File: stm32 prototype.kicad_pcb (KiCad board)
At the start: 2 copper layers, 109 parts, among them J1 USB_B_Mini, J2 Conn_01x06_Male, J3 Conn_01x02, Q1 Q_NMOS_GSD, Q2 Q_NMOS_GSD, Q3 Q_NMOS_GSD, Q4 Q_NMOS_GSD, Q5 Q_NMOS_GSD, Q6 Q_NMOS_GSD, Q7 Q_NMOS_GSD, Q8 Q_NMOS_GSD, Q9 Q_NMOS_GSD, U1 FT232RL, U2 W25Q128JV-DTR, U3 STM32F407VGTx, U4 LD1117S33TR, U5 ESP32, U6 IS25LP016D-JNLE-TR, Y1 Crystal_GND24, Y2 Crystal_GND23, Y3 Crystal_GND23

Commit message: worked on some layout
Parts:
- added C16: 2.2uF, Capacitors_SMD:C_0603, F.Cu at (175.5, 142.2)
- added C38: 2.2uF, Capacitors_SMD:C_0603, F.Cu at (182.5, 125.8)
- added C39: .1uF, Capacitors_SMD:C_0603, F.Cu at (159.5, 138.2)
- added C40: 1uF, Capacitors_SMD:C_0603, F.Cu at (157.5, 138.2)
- added C41: C, Capacitors_SMD:C_0603, F.Cu at (159.5, 131.8)
- added R40: 0R, Resistors_SMD:R_0603, F.Cu at (184.5, 112.2)
- added R41: 0R, Resistors_SMD:R_0603, F.Cu at (186.5, 112.2)
- added R42: 0R, Resistors_SMD:R_0603, F.Cu at (188.5, 112.2)
- added R43: 0R, Resistors_SMD:R_0603, F.Cu at (190.5, 112.2)
- added R44: 0R, Resistors_SMD:R_0603, F.Cu at (192.5, 112.2)
- added R45: 0R, Resistors_SMD:R_0603, F.Cu at (194.5, 112.2)
- added R46: DNP, Resistors_SMD:R_0603, F.Cu at (167.5, 116.2)
- added R47: 10K, Resistors_SMD:R_0603, F.Cu at (165.5, 116.2)
- added R48: 100K, Resistors_SMD:R_0603, F.Cu at (157.5, 132.0)
- C1, C10, C11, C12, C13, C14, C15, C17, C18, C19, C2, C20, C21, C22, C23, C24, C25, C26, C27, C28, C29, C3, C31, C36, C37, C4, C5, C6, C7, C8, C9: footprint Capacitors_SMD:C_0603_HandSoldering -> Capacitors_SMD:C_0603
- D10, D11, D2, D3, D4, D5, D6, D7, D8, D9: footprint LEDs:LED_1206_HandSoldering -> LEDs:LED_1206
- J2: value Conn_01x06_Male -> Conn_01x06
- Q1, Q2, Q3, Q4, Q5, Q6, Q7, Q8: footprint TO_SOT_Packages_SMD:SOT-323_SC-70_Handsoldering -> TO_SOT_Packages_SMD:SOT-323_SC-70
- R1, R10, R11, R12, R13, R14, R15, R16, R17, R18, R19, R2, R20, R21, R22, R23, R24, R25, R3, R34, R35, R36, R4, R5, R6, R7, R8, R9: footprint Resistors_SMD:R_0603_HandSoldering -> Resistors_SMD:R_0603
- moved R1 124.6 mm to (224.0, 92.0)
- moved C1 81.8 mm to (206.8, 130.0)
- moved D6 60.2 mm to (218.0, 83.3), turned to 90 degrees
- moved C15 60.2 mm to (77.0, 114.0), turned to 90 degrees
- moved C14 60.1 mm to (73.0, 114.0), turned to 90 degrees
- moved C13 59.8 mm to (75.0, 114.0), turned to 90 degrees
- moved C8 59.2 mm to (178.5, 142.0), turned to 90 degrees
- moved D7 56.8 mm to (215.0, 83.3), turned to 90 degrees
- moved R4 54.7 mm to (93.9, 119.0)
- moved Q4 52.6 mm to (215.0, 89.5), turned to 90 degrees
- moved R36 51.2 mm to (206.5, 136.0), turned to 180 degrees
- moved R35 51.1 mm to (206.5, 134.0), turned to 180 degrees
- moved D9 50.5 mm to (209.0, 83.3), turned to 90 degrees
- moved C7 50.4 mm to (165.5, 142.0)
- moved Q3 50.3 mm to (218.0, 89.5), turned to 90 degrees
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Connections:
- J2 pad 1: GND -> Net-(J2-Pad1)
- J2 pad 2: /NJTRST -> Net-(J2-Pad2)
- J2 pad 3: /JTDO -> Net-(J2-Pad3)
- J2 pad 4: /JTDI -> Net-(J2-Pad4)
- J2 pad 5: /SWCLK -> Net-(J2-Pad5)
- J2 pad 6: /SWDAT -> Net-(J2-Pad6)
- U3 pad 14: (no net) -> NRST
- U3 pad 21: (no net) -> +3V3
- U3 pad 49: (no net) -> Net-(C16-Pad2)
- U3 pad 72: /SWDAT -> TMS_SWDIO
- U3 pad 73: (no net) -> Net-(C38-Pad2)
- U3 pad 76: /SWCLK -> TCK_SWCLK
- U3 pad 77: /JTDI -> (no net)
- U3 pad 89: /JTDO -> SWO
- U3 pad 90: /NJTRST -> (no net)
- U3 pad 94: (no net) -> Net-(R46-Pad2)
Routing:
- net GND: track 0.00 -> 25.2 mm, vias 0 -> 8
- net +3V3: track 0.00 -> 13.6 mm, vias 0 -> 8
- net Net-(D9-Pad1): track 0.00 -> 2.31 mm
- net Net-(D8-Pad1): track 0.00 -> 2.31 mm
- net Net-(D7-Pad1): track 0.00 -> 2.31 mm
- net Net-(D6-Pad1): track 0.00 -> 2.31 mm
- net Net-(D5-Pad1): track 0.00 -> 2.31 mm
- net Net-(D4-Pad1): track 0.00 -> 2.31 mm
- net Net-(D11-Pad1): track 0.00 -> 2.31 mm
- net Net-(D10-Pad1): track 0.00 -> 2.31 mm
- net Net-(Q8-Pad3): track 0.00 -> 1.81 mm
- net Net-(Q7-Pad3): track 0.00 -> 1.81 mm
- net Net-(Q6-Pad3): track 0.00 -> 1.81 mm
- net Net-(Q5-Pad3): track 0.00 -> 1.81 mm
- net Net-(Q4-Pad3): track 0.00 -> 1.81 mm
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- added copper zone on In2.Cu, net +3V3
- added copper zone on In1.Cu, net GND
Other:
- copper layers 2 -> 4

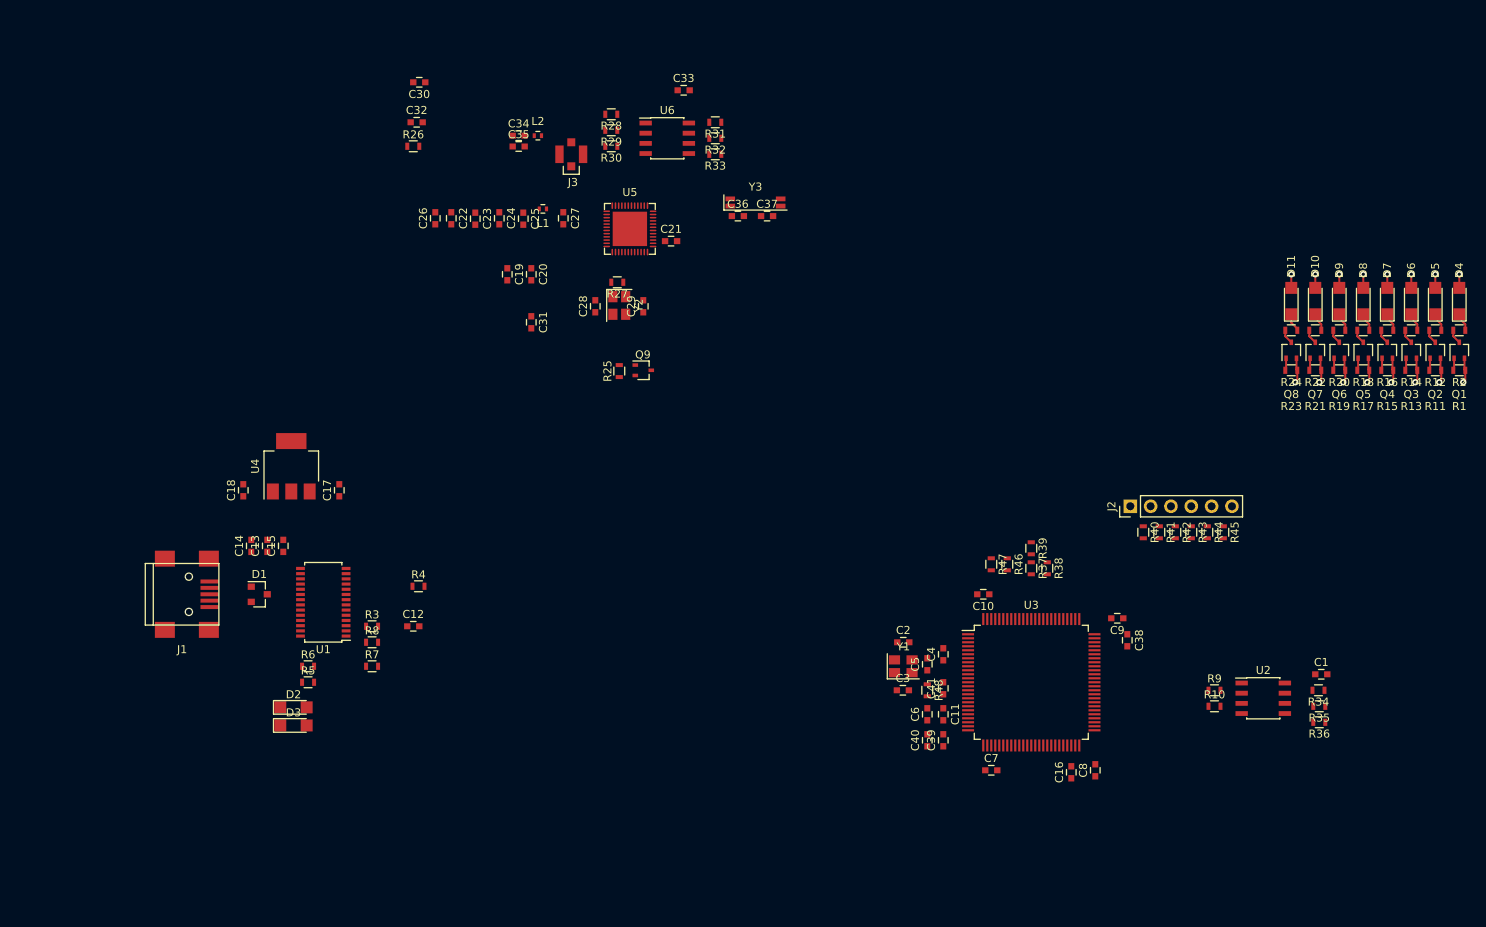
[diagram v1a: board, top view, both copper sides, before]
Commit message: laid out usb input section
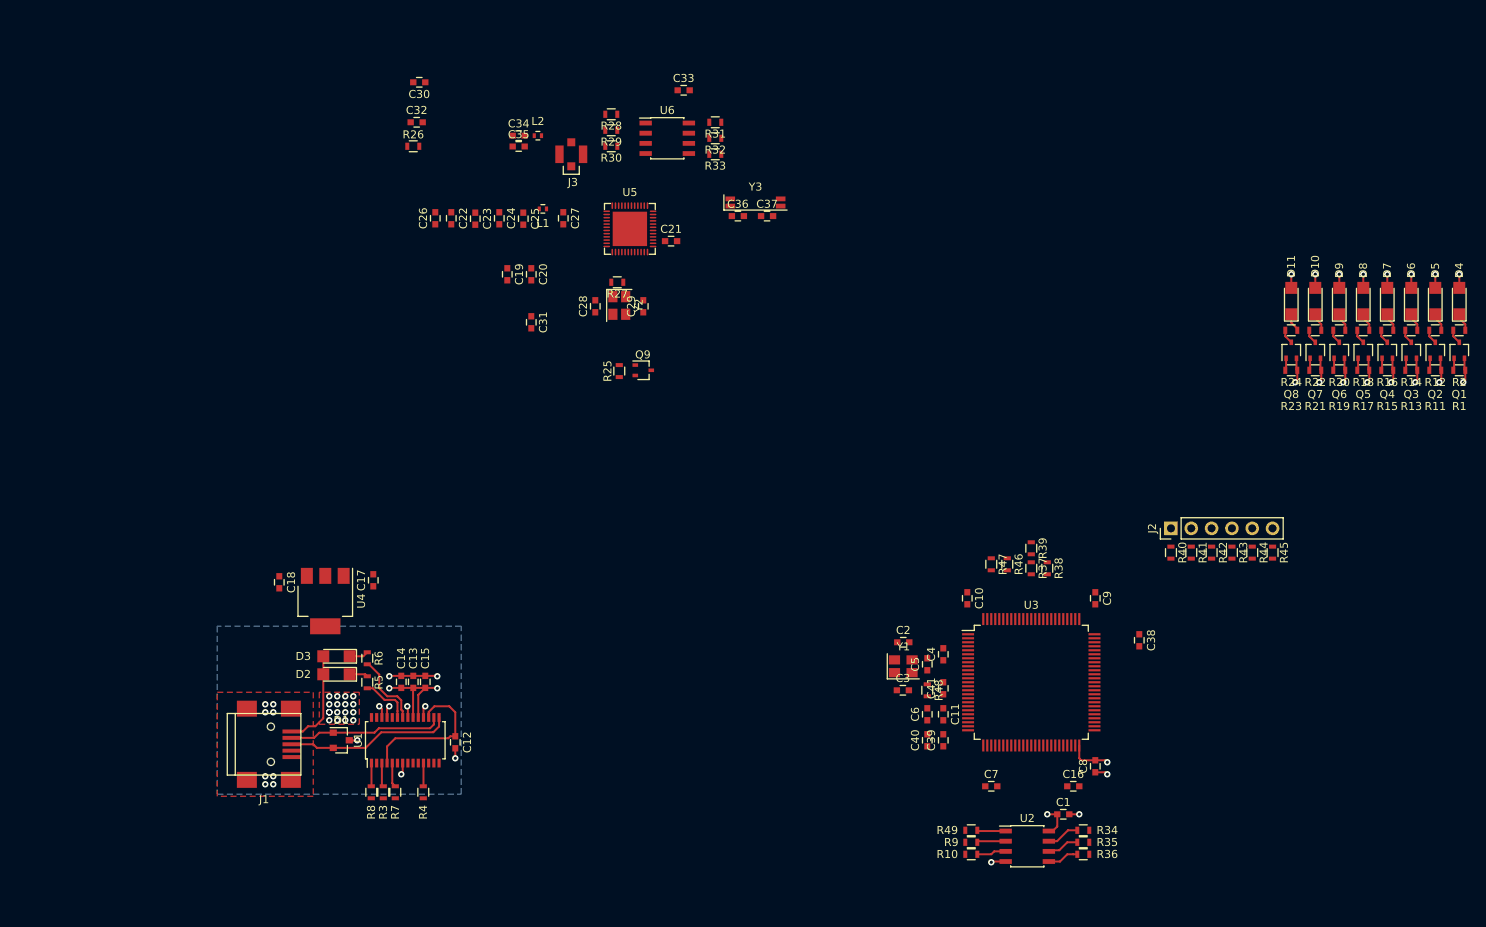
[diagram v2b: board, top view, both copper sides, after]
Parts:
- added R49: 0R, Resistors_SMD:R_0603, F.Cu at (163.0, 149.5)
- moved C1 36.7 mm to (174.5, 147.5)
- moved R9 35.8 mm to (163.0, 151.0)
- moved R10 35.6 mm to (163.0, 152.5)
- moved U2 34.8 mm to (170.0, 151.5)
- moved R34 34.2 mm to (177.0, 149.5)
- moved R35 34.0 mm to (177.0, 151.0)
- moved R36 33.8 mm to (177.0, 152.5)
- moved R4 25.8 mm to (94.5, 144.8), turned to 90 degrees
- moved C14 25.3 mm to (91.8, 130.9)
- moved C13 24.9 mm to (93.2, 130.9)
- moved C15 24.6 mm to (94.8, 130.9)
- moved J1 21.4 mm to (75.2, 138.8)
- moved D1 20.9 mm to (84.2, 138.2)
- moved R3 20.8 mm to (89.5, 144.8), turned to 90 degrees
- moved U1 20.1 mm to (92.2, 138.2), turned to 90 degrees
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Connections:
- J1 pad 2: Net-(D1-Pad2) -> Net-(D1-Pad1)
- J1 pad 3: Net-(D1-Pad1) -> Net-(D1-Pad2)
- U1 pad 15: Net-(D1-Pad1) -> Net-(D1-Pad2)
- U1 pad 16: Net-(D1-Pad2) -> Net-(D1-Pad1)
- U2 pad 1: MEM_CHIP_SELECT -> Net-(R49-Pad2)
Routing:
- net +5V: track 0.00 -> 26.2 mm, vias 0 -> 20
- net Net-(D1-Pad2): track 0.00 -> 20.8 mm
- net GND: track 25.2 -> 45.6 mm, vias 8 -> 28
- net Net-(D1-Pad1): track 0.00 -> 19.3 mm
- net Net-(C12-Pad1): track 0.00 -> 18.7 mm
- net +3V3: track 13.6 -> 23.0 mm, vias 8 -> 10
- net Net-(R6-Pad2): track 0.00 -> 9.33 mm
- net Net-(R5-Pad2): track 0.00 -> 6.39 mm
- net Net-(R34-Pad2): track 0.00 -> 4.12 mm
- net Net-(R35-Pad2): track 0.00 -> 4.02 mm
- net Net-(R36-Pad2): track 0.00 -> 3.92 mm
- net Net-(R10-Pad2): track 0.00 -> 3.70 mm
- net Net-(R9-Pad2): track 0.00 -> 3.61 mm
- net Net-(R49-Pad2): track 0.00 -> 3.59 mm
- net FTDI_RXD: track 0.00 -> 3.06 mm
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- added copper zone on B.Cu, net +5V
- added copper zone on F.Cu, net +5V
- added copper zone on F.Cu, net GND

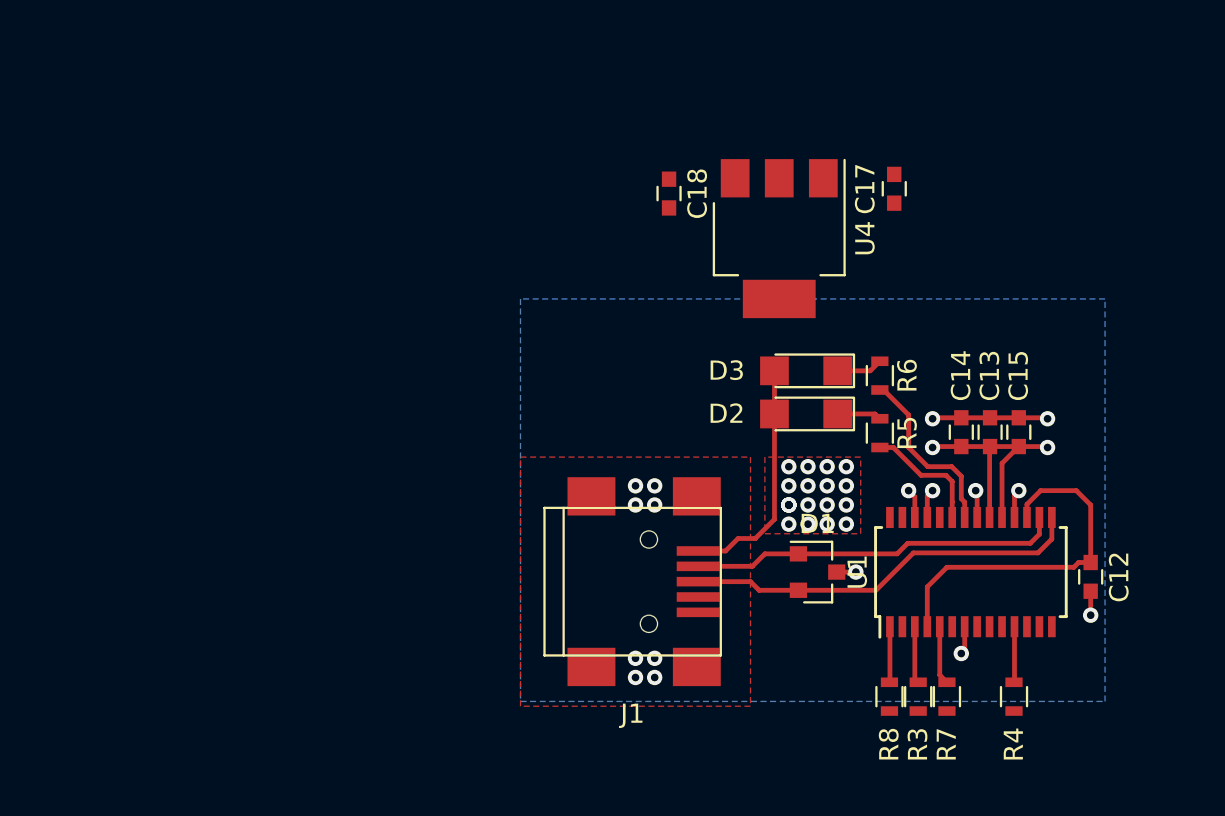
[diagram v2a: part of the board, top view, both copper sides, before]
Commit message: added switcher to 3.3v rail, began layout of 3.3v regulator
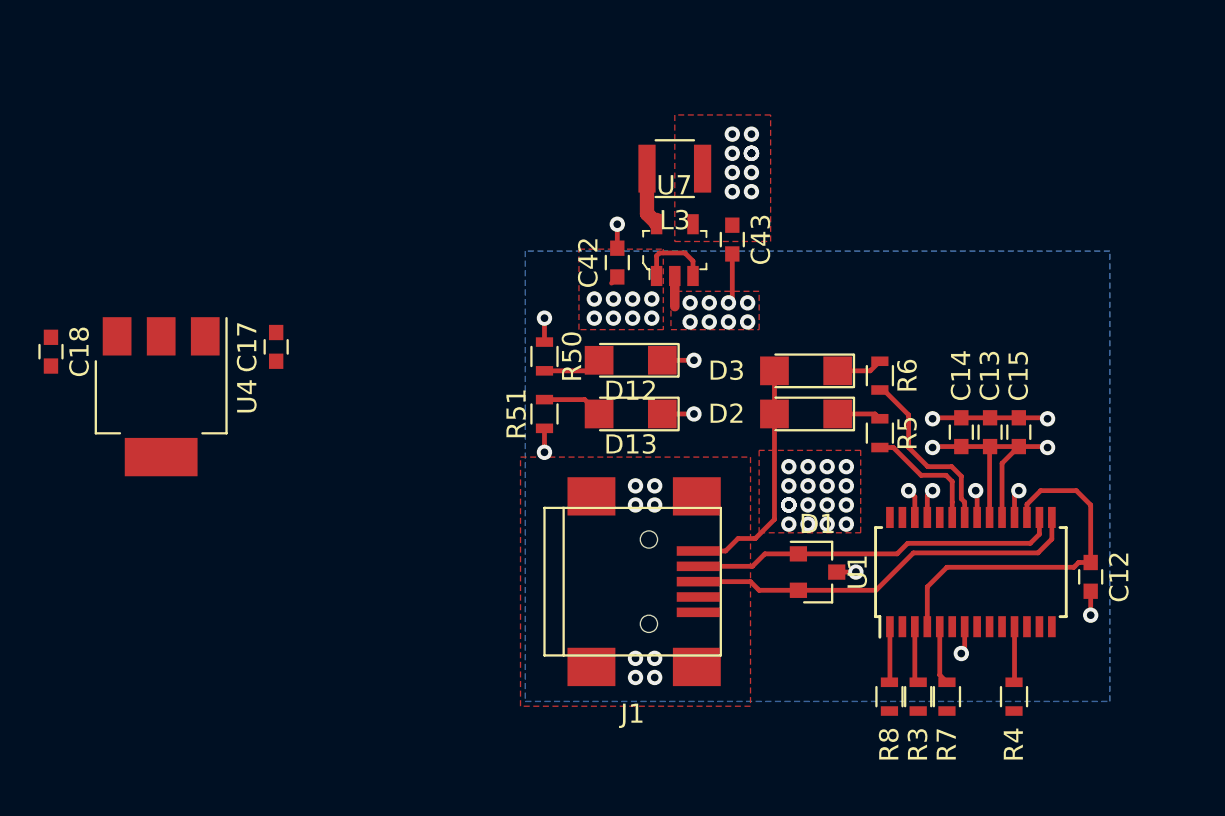
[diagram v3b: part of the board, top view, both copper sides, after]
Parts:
- added C42: 4.7uF, Capacitors_SMD:C_0603, F.Cu at (73.8, 122.1)
- added C43: 10uF, Capacitors_SMD:C_0603, F.Cu at (79.8, 120.9)
- added D12: LED, LEDs:LED_1206, F.Cu at (74.5, 127.2)
- added D13: LED, LEDs:LED_1206, F.Cu at (74.5, 130.0)
- added L3: 10uH, Inductors_SMD:L_1210, F.Cu at (76.8, 117.2)
- added R50: 330R, Resistors_SMD:R_0603, F.Cu at (70.0, 127.0)
- added R51: 330R, Resistors_SMD:R_0603, F.Cu at (70.0, 130.0)
- added U7: TPS62203DBVR, digikey-footprints:SOT-753, F.Cu at (76.8, 121.5)
- moved C17 33.3 mm to (56.0, 126.5)
- moved C18 33.3 mm to (44.2, 126.8)
- moved U4 33.3 mm to (50.0, 129.1)
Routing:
- net GND: track 45.6 -> 54.4 mm, vias 28 -> 39
- net +5V: track 26.2 -> 31.9 mm, vias 20 -> 29
- net Net-(L3-Pad2): track 0.00 -> 3.33 mm
- net Net-(D13-Pad2): track 0.00 -> 3.16 mm
- net Net-(D12-Pad2): track 0.00 -> 3.08 mm
- net +3V3: track 23.0 -> 24.2 mm, vias 10 -> 21
- added copper zone on F.Cu, net +3V3

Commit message: worked on some layout around the stm32f
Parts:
- added J4: Conn_01x10, Pin_Headers:Pin_Header_Straight_1x10_Pitch2.54mm, F.Cu at (86.0, 151.0)
- moved D4 78.9 mm to (187.8, 153.4), turned to 270 degrees
- moved D5 76.3 mm to (190.8, 153.4), turned to 270 degrees
- moved D6 74.2 mm to (193.8, 153.4), turned to 270 degrees
- moved R2 72.5 mm to (187.8, 149.8), turned to 0 degrees
- moved D7 72.4 mm to (196.8, 153.4), turned to 270 degrees
- moved D8 71.2 mm to (199.8, 153.4), turned to 270 degrees
- moved D9 70.4 mm to (202.8, 153.4), turned to 270 degrees
- moved D11 70.3 mm to (208.8, 153.4), turned to 270 degrees
- moved D10 70.1 mm to (205.8, 153.4), turned to 270 degrees
- moved R12 69.7 mm to (190.8, 149.8), turned to 0 degrees
- moved Q1 68.2 mm to (187.8, 147.3), turned to 270 degrees
- moved R14 67.3 mm to (193.8, 149.8), turned to 0 degrees
- moved R16 65.4 mm to (196.8, 149.8), turned to 0 degrees
- moved Q2 65.2 mm to (190.8, 147.3), turned to 270 degrees
- moved R1 64.0 mm to (187.8, 144.8), turned to 180 degrees
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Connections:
- U1 pad 10: (no net) -> FTDI_DCD
- U1 pad 12: (no net) -> FTDI_CBUS4
- U1 pad 13: (no net) -> FTDI_CBUS2
- U1 pad 14: (no net) -> FTDI_CBUS3
- U1 pad 2: (no net) -> FTDI_DTR
- U1 pad 6: (no net) -> FTDI_RI
- U1 pad 9: (no net) -> FTDI_DCR
- U3 pad 39: (no net) -> STATUS_BIT7
- U3 pad 40: (no net) -> STATUS_BIT6
- U3 pad 41: (no net) -> STATUS_BIT5
- U3 pad 42: (no net) -> STATUS_BIT4
- U3 pad 43: (no net) -> STATUS_BIT3
- U3 pad 44: (no net) -> STATUS_BIT2
- U3 pad 45: (no net) -> STATUS_BIT1
- U3 pad 46: (no net) -> STATUS_BIT0
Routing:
- net (no net): track 0.00 -> 149.8 mm
- net SWO: track 0.00 -> 35.7 mm, vias 0 -> 2
- net +3V3: track 24.2 -> 49.8 mm, vias 21 -> 26
- net GND: track 54.4 -> 79.6 mm, vias 39 -> 46
- net TMS_SWDIO: track 0.00 -> 18.4 mm
- net TCK_SWCLK: track 0.00 -> 10.1 mm
- net Net-(R46-Pad2): track 0.00 -> 10.1 mm
- net ESP32_RXD: track 0.00 -> 7.47 mm
- net ESP32_TXD: track 0.00 -> 6.85 mm
- net Net-(C38-Pad2): track 0.00 -> 5.81 mm
- net Net-(C16-Pad2): track 0.00 -> 5.31 mm
- net Net-(J2-Pad6): track 0.00 -> 2.28 mm
- net Net-(J2-Pad5): track 0.00 -> 2.28 mm
- net Net-(J2-Pad4): track 0.00 -> 2.28 mm
- net Net-(J2-Pad3): track 0.00 -> 2.28 mm
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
